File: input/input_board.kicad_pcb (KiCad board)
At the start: 4 copper layers, 271.6 x 100 mm, 233 parts, among them J1 Sensor, J101 Gain, J102 +IN, J103 -IN, J2 SCKB, J3 Decimate, J4 SCKA, J5 MCLK, J6 SDOB1, P1 my_pcie_8x, Q1 NSS1C300ET4G, Q2 2STD1665T4, Q3 NSS1C300ET4G, U1 DS90LV048, U101 AD8599, U102 LTC2512-24, U104 THS4131, U2 FIN1047, U3 OP27, U4 OPA830, U5 74LVC541A, U6 OPA830, U7 MCP1755S-3302E/DB, U8 NCP1117STAT3G, U9 OPA1679, X1 channel_dummy, X2 channel_dummy

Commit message: Input board is nearly ready to send off for the first spin.
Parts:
- removed X1, X2: channel_dummy, input:channel_dummy
- added C201: 330uF, Capacitor_SMD:CP_Elec_8x6.7, F.Cu at (118.2, 106.0)
- added C202: 330uF, Capacitor_SMD:CP_Elec_8x6.7, F.Cu at (118.2, 90.0)
- added C203: 33nF, Capacitor_SMD:C_0805_2012Metric, F.Cu at (133.8, 98.0)
- added C204: 1uF, Capacitor_SMD:C_0805_2012Metric, F.Cu at (142.0, 105.0)
- added C205: 2.2nF, Capacitor_SMD:C_0603_1608Metric, F.Cu at (136.6, 90.4)
- added C206: 2.2nF, Capacitor_SMD:C_0603_1608Metric, F.Cu at (136.6, 105.6)
- added C207: 1uF, Capacitor_SMD:C_0805_2012Metric, F.Cu at (150.0, 98.0)
- added C208: 1uF, Capacitor_SMD:C_0805_2012Metric, F.Cu at (145.6, 105.0)
- added C209: 1uF, Capacitor_SMD:C_0805_2012Metric, F.Cu at (145.5, 91.0)
- added C210: 1uF, Capacitor_SMD:C_0805_2012Metric, F.Cu at (152.0, 88.2)
- added C211: 1uF, Capacitor_SMD:C_0805_2012Metric, F.Cu at (152.0, 107.8)
- added C212: 1nF, Capacitor_SMD:C_0805_2012Metric, F.Cu at (43.5, 96.8)
- added C213: 1nF, Capacitor_SMD:C_0805_2012Metric, F.Cu at (43.5, 99.3)
- added C214: 3.3nF, Capacitor_SMD:C_0805_2012Metric, F.Cu at (75.0, 95.0)
- added C215: 1uF, Capacitor_SMD:C_0805_2012Metric, F.Cu at (78.8, 86.6)
- added C216: 1uF, Capacitor_SMD:C_0805_2012Metric, F.Cu at (81.2, 86.6)
- added C217: 1uF, Capacitor_SMD:C_0805_2012Metric, F.Cu at (81.2, 109.4)
- added C218: 1uF, Capacitor_SMD:C_0805_2012Metric, F.Cu at (78.8, 109.4)
- added C219: 1nF, Capacitor_SMD:C_0805_2012Metric, F.Cu at (85.2, 94.0)
- added C220: 1nF, Capacitor_SMD:C_0805_2012Metric, F.Cu at (85.2, 102.0)
- added C221: 2.2nF, Capacitor_SMD:C_0603_1608Metric, F.Cu at (92.4, 107.0)
- added C222: 2.2nF, Capacitor_SMD:C_0603_1608Metric, F.Cu at (93.6, 90.6)
- added C223: 1uF, Capacitor_SMD:C_0805_2012Metric, F.Cu at (98.2, 98.0)
- added C224: 1uF, Capacitor_SMD:C_0805_2012Metric, F.Cu at (90.6, 91.2)
- added C225: 1uF, Capacitor_SMD:C_0805_2012Metric, F.Cu at (95.6, 105.2)
- added C226: OPT, Capacitor_SMD:C_0805_2012Metric, F.Cu at (163.6, 92.6)
- added C227: 6.8nF, Capacitor_SMD:C_0805_2012Metric, F.Cu at (166.4, 90.4)
- added C228: 6.8nF, Capacitor_SMD:C_0805_2012Metric, F.Cu at (166.4, 94.8)
- added C229: 10uF, Capacitor_SMD:C_0603_1608Metric, F.Cu at (182.4, 88.8)
- added C230: 10uF, Capacitor_SMD:C_0603_1608Metric, F.Cu at (173.0, 89.4)
- added C231: 100nF, Capacitor_SMD:C_0603_1608Metric, F.Cu at (182.4, 90.6)
- added C232: 100nF, Capacitor_SMD:C_0603_1608Metric, F.Cu at (173.0, 91.4)
- added C233: 100nF, Capacitor_SMD:C_0603_1608Metric, F.Cu at (172.9, 94.4)
- added C234: 47uF, Capacitor_SMD:C_1210_3225Metric, F.Cu at (171.9, 96.9)
- added C235: 330uF, Capacitor_SMD:CP_Elec_8x6.7, F.Cu at (174.6, 106.0)
- added C301: 330uF, Capacitor_SMD:CP_Elec_8x6.7, F.Cu at (118.2, 141.1)
- added C302: 330uF, Capacitor_SMD:CP_Elec_8x6.7, F.Cu at (118.2, 125.0)
- added C303: 33nF, Capacitor_SMD:C_0805_2012Metric, F.Cu at (133.8, 133.0)
- added C304: 1uF, Capacitor_SMD:C_0805_2012Metric, F.Cu at (142.0, 140.0)
- added C305: 2.2nF, Capacitor_SMD:C_0603_1608Metric, F.Cu at (136.6, 125.4)
- added C306: 2.2nF, Capacitor_SMD:C_0603_1608Metric, F.Cu at (136.6, 140.6)
- added C307: 1uF, Capacitor_SMD:C_0805_2012Metric, F.Cu at (150.0, 133.0)
- added C308: 1uF, Capacitor_SMD:C_0805_2012Metric, F.Cu at (145.6, 140.0)
- added C309: 1uF, Capacitor_SMD:C_0805_2012Metric, F.Cu at (145.5, 126.0)
- added C310: 1uF, Capacitor_SMD:C_0805_2012Metric, F.Cu at (152.0, 123.2)
- added C311: 1uF, Capacitor_SMD:C_0805_2012Metric, F.Cu at (152.0, 142.8)
- added C312: 1nF, Capacitor_SMD:C_0805_2012Metric, F.Cu at (43.5, 131.8)
- added C313: 1nF, Capacitor_SMD:C_0805_2012Metric, F.Cu at (43.5, 134.3)
- added C314: 3.3nF, Capacitor_SMD:C_0805_2012Metric, F.Cu at (75.0, 130.0)
- added C315: 1uF, Capacitor_SMD:C_0805_2012Metric, F.Cu at (78.8, 121.6)
- added C316: 1uF, Capacitor_SMD:C_0805_2012Metric, F.Cu at (81.2, 121.6)
- added C317: 1uF, Capacitor_SMD:C_0805_2012Metric, F.Cu at (81.2, 144.4)
- added C318: 1uF, Capacitor_SMD:C_0805_2012Metric, F.Cu at (78.8, 144.4)
- added C319: 1nF, Capacitor_SMD:C_0805_2012Metric, F.Cu at (85.2, 129.0)
- added C320: 1nF, Capacitor_SMD:C_0805_2012Metric, F.Cu at (85.2, 137.0)
- added C321: 2.2nF, Capacitor_SMD:C_0603_1608Metric, F.Cu at (92.4, 142.0)
- added C322: 2.2nF, Capacitor_SMD:C_0603_1608Metric, F.Cu at (93.6, 125.6)
- added C323: 1uF, Capacitor_SMD:C_0805_2012Metric, F.Cu at (98.2, 133.0)
- added C324: 1uF, Capacitor_SMD:C_0805_2012Metric, F.Cu at (90.6, 126.2)
- added C325: 1uF, Capacitor_SMD:C_0805_2012Metric, F.Cu at (95.6, 140.2)
- added C326: OPT, Capacitor_SMD:C_0805_2012Metric, F.Cu at (163.6, 127.6)
- added C327: 6.8nF, Capacitor_SMD:C_0805_2012Metric, F.Cu at (166.4, 125.4)
- added C328: 6.8nF, Capacitor_SMD:C_0805_2012Metric, F.Cu at (166.4, 129.8)
- added C329: 10uF, Capacitor_SMD:C_0603_1608Metric, F.Cu at (182.4, 123.8)
- added C330: 10uF, Capacitor_SMD:C_0603_1608Metric, F.Cu at (173.0, 124.4)
- added C331: 100nF, Capacitor_SMD:C_0603_1608Metric, F.Cu at (182.4, 125.6)
- added C332: 100nF, Capacitor_SMD:C_0603_1608Metric, F.Cu at (173.0, 126.4)
- added C333: 100nF, Capacitor_SMD:C_0603_1608Metric, F.Cu at (172.9, 129.4)
- added C334: 47uF, Capacitor_SMD:C_1210_3225Metric, F.Cu at (171.9, 131.9)
- added C335: 330uF, Capacitor_SMD:CP_Elec_8x6.7, F.Cu at (174.6, 142.0)
- added D201: BAS21S, Package_TO_SOT_SMD:SOT-23, F.Cu at (152.0, 104.4)
- added D202: 5V (standoff), Diode_SMD:D_SMA, F.Cu at (167.0, 107.0)
- added D203: 12V, Diode_SMD:D_SOD-323, F.Cu at (55.0, 94.2)
- added D204: 12V, Diode_SMD:D_SOD-323, F.Cu at (55.0, 101.8)
- added D205: BAS21S, Package_TO_SOT_SMD:SOT-23, F.Cu at (80.0, 90.8)
- added D206: BAS21S, Package_TO_SOT_SMD:SOT-23, F.Cu at (80.0, 105.2)
- added D207: BAS21S, Package_TO_SOT_SMD:SOT-23, F.Cu at (64.0, 108.4)
- added D208: BAS21S, Package_TO_SOT_SMD:SOT-23, F.Cu at (59.8, 108.4)
- added D209: BAS21S, Package_TO_SOT_SMD:SOT-23, F.Cu at (64.0, 87.6)
- added D210: BAS21S, Package_TO_SOT_SMD:SOT-23, F.Cu at (59.8, 87.6)
- added D211: BAS21S, Package_TO_SOT_SMD:SOT-23, F.Cu at (152.0, 91.6)
- added D301: BAS21S, Package_TO_SOT_SMD:SOT-23, F.Cu at (152.0, 126.6)
- added D302: BAS21S, Package_TO_SOT_SMD:SOT-23, F.Cu at (152.0, 139.4)
- added D303: 5V (standoff), Diode_SMD:D_SMA, F.Cu at (166.6, 143.0)
- added D304: 12V, Diode_SMD:D_SOD-323, F.Cu at (55.0, 129.2)
- added D305: 12V, Diode_SMD:D_SOD-323, F.Cu at (55.0, 136.8)
- added D306: BAS21S, Package_TO_SOT_SMD:SOT-23, F.Cu at (80.0, 125.8)
- added D307: BAS21S, Package_TO_SOT_SMD:SOT-23, F.Cu at (80.0, 140.2)
- added D308: BAS21S, Package_TO_SOT_SMD:SOT-23, F.Cu at (64.0, 143.4)
- added D309: BAS21S, Package_TO_SOT_SMD:SOT-23, F.Cu at (59.8, 143.4)
- added D310: BAS21S, Package_TO_SOT_SMD:SOT-23, F.Cu at (64.0, 122.6)
- added D311: BAS21S, Package_TO_SOT_SMD:SOT-23, F.Cu at (59.8, 122.6)
- added E201: 2036-07-SMLF, input:GDT_3LINE_Bourns_2036-xx-SM, F.Cu at (36.0, 98.0)
- added E301: 2036-07-SMLF, input:GDT_3LINE_Bourns_2036-xx-SM, F.Cu at (36.0, 133.0)
- added FB201: 21 Ohm, Inductor_SMD:L_0805_2012Metric, F.Cu at (125.2, 91.8)
- added FB202: 21 Ohm, Inductor_SMD:L_0805_2012Metric, F.Cu at (111.4, 107.8)
- added FB203: 2K Ohm, Inductor_SMD:L_0805_2012Metric, F.Cu at (43.5, 94.5)
- added FB204: 2K Ohm, Inductor_SMD:L_0805_2012Metric, F.Cu at (43.5, 101.5)
- added FB205: 21 Ohm, Inductor_SMD:L_0805_2012Metric, F.Cu at (181.4, 109.2)
- added FB301: 21 Ohm, Inductor_SMD:L_0805_2012Metric, F.Cu at (125.2, 126.8)
- added FB302: 21 Ohm, Inductor_SMD:L_0805_2012Metric, F.Cu at (111.4, 142.8)
- added FB303: 2K Ohm, Inductor_SMD:L_0805_2012Metric, F.Cu at (43.5, 129.5)
- added FB304: 2K Ohm, Inductor_SMD:L_0805_2012Metric, F.Cu at (43.5, 136.5)
- added FB305: 21 Ohm, Inductor_SMD:L_0805_2012Metric, F.Cu at (181.4, 144.2)
- added FL201: 4.7mH, input:L_CommonMode_Bourns_DR331, F.Cu at (52.2, 98.0)
- added FL301: 4.7mH, input:L_CommonMode_Bourns_DR331, F.Cu at (52.2, 133.0)
- added J201: Gain, Connector_PinHeader_2.00mm:PinHeader_2x02_P2.00mm_Vertical_SMD, F.Cu at (105.2, 98.0)
- added J202: +IN, Connector_Coaxial:MMCX_Molex_73415-1471_Vertical, F.Cu at (158.5, 87.5)
- added J203: -IN, Connector_Coaxial:MMCX_Molex_73415-1471_Vertical, F.Cu at (158.5, 99.0)
- added J301: Gain, Connector_PinHeader_2.00mm:PinHeader_2x02_P2.00mm_Vertical_SMD, F.Cu at (105.2, 133.0)
- added J302: +IN, Connector_Coaxial:MMCX_Molex_73415-1471_Vertical, F.Cu at (158.5, 122.5)
- added J303: -IN, Connector_Coaxial:MMCX_Molex_73415-1471_Vertical, F.Cu at (158.5, 134.0)
- added R201: 1K, Resistor_SMD:R_0603_1608Metric, F.Cu at (130.0, 93.2)
- added R202: 1K, Resistor_SMD:R_0603_1608Metric, F.Cu at (130.0, 102.8)
- added R203: 698, Resistor_SMD:R_0603_1608Metric, F.Cu at (130.0, 91.0)
- added R204: 698, Resistor_SMD:R_0603_1608Metric, F.Cu at (136.6, 103.4)
- added R205: 3.3K, Resistor_SMD:R_0603_1608Metric, F.Cu at (142.6, 109.2)
- added R206: 3.3K, Resistor_SMD:R_0603_1608Metric, F.Cu at (138.6, 109.2)
- added R207: 1K, Resistor_SMD:R_0603_1608Metric, F.Cu at (136.6, 92.6)
- added R208: 1K, Resistor_SMD:R_0603_1608Metric, F.Cu at (130.0, 105.0)
- added R209: 10, Resistor_SMD:R_0805_2012Metric, F.Cu at (67.6, 93.8)
- added R210: 10, Resistor_SMD:R_0805_2012Metric, F.Cu at (67.6, 102.4)
- added R211: 10, Resistor_SMD:R_0805_2012Metric, F.Cu at (71.6, 93.8)
- added R212: 10, Resistor_SMD:R_0805_2012Metric, F.Cu at (71.6, 102.4)
- added R213: 200K, Resistor_SMD:R_0603_1608Metric, F.Cu at (73.0, 90.8)
- added R214: 200K, Resistor_SMD:R_0603_1608Metric, F.Cu at (69.6, 90.8)
- added R215: 200K, Resistor_SMD:R_0603_1608Metric, F.Cu at (73.0, 105.2)
- added R216: 200K, Resistor_SMD:R_0603_1608Metric, F.Cu at (69.6, 105.2)
- added R217: 200, Resistor_SMD:R_0603_1608Metric, F.Cu at (75.0, 100.6)
- added R218: 10K, Resistor_SMD:R_0603_1608Metric, F.Cu at (69.6, 108.6)
- added R219: 10K, Resistor_SMD:R_0603_1608Metric, F.Cu at (73.0, 108.6)
- added R220: 10K, Resistor_SMD:R_0603_1608Metric, F.Cu at (69.6, 87.4)
- added R221: 10K, Resistor_SMD:R_0603_1608Metric, F.Cu at (73.0, 87.4)
- added R222: 10, Resistor_SMD:R_0805_2012Metric, F.Cu at (81.0, 94.4)
- added R223: 10, Resistor_SMD:R_0805_2012Metric, F.Cu at (81.0, 101.6)
- added R224: 100, Resistor_SMD:R_0603_1608Metric, F.Cu at (107.2, 92.0)
- added R225: 243, Resistor_SMD:R_0603_1608Metric, F.Cu at (103.6, 92.0)
- added R226: 1K, Resistor_SMD:R_0603_1608Metric, F.Cu at (101.0, 98.0)
- added R227: 499, Resistor_SMD:R_0805_2012Metric, F.Cu at (92.4, 104.6)
- added R228: 499, Resistor_SMD:R_0805_2012Metric, F.Cu at (93.8, 88.4)
- added R229: 10, Resistor_SMD:R_0805_2012Metric, F.Cu at (163.6, 88.2)
- added R230: 10, Resistor_SMD:R_0805_2012Metric, F.Cu at (163.6, 96.8)
- added R231: GND lift, Resistor_SMD:R_0603_1608Metric, F.Cu at (158.4, 103.0)
- added R232: 33, Resistor_SMD:R_0603_1608Metric, F.Cu at (187.6, 93.7)
- added R233: 33, Resistor_SMD:R_0603_1608Metric, F.Cu at (184.0, 92.6)
- added R301: 1K, Resistor_SMD:R_0603_1608Metric, F.Cu at (130.0, 128.2)
- added R302: 1K, Resistor_SMD:R_0603_1608Metric, F.Cu at (130.0, 137.8)
- added R303: 698, Resistor_SMD:R_0603_1608Metric, F.Cu at (130.0, 126.0)
- added R304: 698, Resistor_SMD:R_0603_1608Metric, F.Cu at (136.6, 138.4)
- added R305: 3.3K, Resistor_SMD:R_0603_1608Metric, F.Cu at (142.6, 144.2)
- added R306: 3.3K, Resistor_SMD:R_0603_1608Metric, F.Cu at (138.6, 144.2)
- added R307: 1K, Resistor_SMD:R_0603_1608Metric, F.Cu at (136.6, 127.6)
- added R308: 1K, Resistor_SMD:R_0603_1608Metric, F.Cu at (130.0, 140.0)
- added R309: 10, Resistor_SMD:R_0805_2012Metric, F.Cu at (67.6, 128.8)
- added R310: 10, Resistor_SMD:R_0805_2012Metric, F.Cu at (67.6, 137.4)
- added R311: 10, Resistor_SMD:R_0805_2012Metric, F.Cu at (71.6, 128.8)
- added R312: 10, Resistor_SMD:R_0805_2012Metric, F.Cu at (71.6, 137.4)
- added R313: 200K, Resistor_SMD:R_0603_1608Metric, F.Cu at (73.0, 125.8)
- added R314: 200K, Resistor_SMD:R_0603_1608Metric, F.Cu at (69.6, 125.8)
- added R315: 200K, Resistor_SMD:R_0603_1608Metric, F.Cu at (73.0, 140.2)
- added R316: 200K, Resistor_SMD:R_0603_1608Metric, F.Cu at (69.6, 140.2)
- added R317: 200, Resistor_SMD:R_0603_1608Metric, F.Cu at (75.0, 135.6)
- added R318: 10K, Resistor_SMD:R_0603_1608Metric, F.Cu at (69.6, 143.6)
- added R319: 10K, Resistor_SMD:R_0603_1608Metric, F.Cu at (73.0, 143.6)
- added R320: 10K, Resistor_SMD:R_0603_1608Metric, F.Cu at (69.6, 122.4)
- added R321: 10K, Resistor_SMD:R_0603_1608Metric, F.Cu at (73.0, 122.4)
- added R322: 10, Resistor_SMD:R_0805_2012Metric, F.Cu at (81.0, 129.4)
- added R323: 10, Resistor_SMD:R_0805_2012Metric, F.Cu at (81.0, 136.6)
- added R324: 100, Resistor_SMD:R_0603_1608Metric, F.Cu at (107.2, 127.0)
- added R325: 243, Resistor_SMD:R_0603_1608Metric, F.Cu at (103.6, 127.0)
- added R326: 1K, Resistor_SMD:R_0603_1608Metric, F.Cu at (101.0, 133.0)
- added R327: 499, Resistor_SMD:R_0805_2012Metric, F.Cu at (92.4, 139.6)
- added R328: 499, Resistor_SMD:R_0805_2012Metric, F.Cu at (93.8, 123.4)
- added R329: 10, Resistor_SMD:R_0805_2012Metric, F.Cu at (163.6, 123.2)
- added R330: 10, Resistor_SMD:R_0805_2012Metric, F.Cu at (163.6, 131.8)
- added R331: GND lift, Resistor_SMD:R_0603_1608Metric, F.Cu at (158.4, 138.0)
- added R332: 33, Resistor_SMD:R_0603_1608Metric, F.Cu at (184.0, 129.4)
- added R333: 33, Resistor_SMD:R_0603_1608Metric, F.Cu at (184.0, 127.6)
- added TP201: +IN2, TestPoint:TestPoint_THTPad_D1.5mm_Drill0.7mm, F.Cu at (129.5, 86.8)
- added TP202: -IN2, TestPoint:TestPoint_THTPad_D1.5mm_Drill0.7mm, F.Cu at (129.5, 109.0)
- added TP203: -IN1, TestPoint:TestPoint_THTPad_D1.5mm_Drill0.7mm, F.Cu at (86.0, 108.2)
- added TP204: +IN1, TestPoint:TestPoint_THTPad_D1.5mm_Drill0.7mm, F.Cu at (86.0, 87.8)
- added TP205: DRL, TestPoint:TestPoint_THTPad_D1.5mm_Drill0.7mm, F.Cu at (179.4, 99.8)
- added TP206: BUSY, TestPoint:TestPoint_THTPad_D1.5mm_Drill0.7mm, F.Cu at (179.4, 86.4)
- added TP207: GND, TestPoint:TestPoint_THTPad_D1.5mm_Drill0.7mm, F.Cu at (159.2, 93.2)
- added TP208: VREF, TestPoint:TestPoint_THTPad_D1.5mm_Drill0.7mm, F.Cu at (168.3, 102.0)
- added TP209: SDOA, TestPoint:TestPoint_THTPad_D1.5mm_Drill0.7mm, F.Cu at (189.5, 90.0)
- added TP301: +IN2, TestPoint:TestPoint_THTPad_D1.5mm_Drill0.7mm, F.Cu at (129.5, 121.8)
- added TP302: -IN2, TestPoint:TestPoint_THTPad_D1.5mm_Drill0.7mm, F.Cu at (129.5, 144.0)
- added TP303: -IN1, TestPoint:TestPoint_THTPad_D1.5mm_Drill0.7mm, F.Cu at (86.0, 143.2)
- added TP304: +IN1, TestPoint:TestPoint_THTPad_D1.5mm_Drill0.7mm, F.Cu at (86.0, 122.8)
- added TP305: DRL, TestPoint:TestPoint_THTPad_D1.5mm_Drill0.7mm, F.Cu at (179.4, 134.8)
- added TP306: BUSY, TestPoint:TestPoint_THTPad_D1.5mm_Drill0.7mm, F.Cu at (179.4, 121.4)
- added TP307: GND, TestPoint:TestPoint_THTPad_D1.5mm_Drill0.7mm, F.Cu at (159.2, 128.2)
- added TP308: VREF, TestPoint:TestPoint_THTPad_D1.5mm_Drill0.7mm, F.Cu at (168.3, 137.0)
- added TP309: SDOA, TestPoint:TestPoint_THTPad_D1.5mm_Drill0.7mm, F.Cu at (193.0, 133.8)
- added U201: THS4131, Package_SO:SO-8_5.3x6.2mm_P1.27mm, F.Cu at (144.9, 98.0)
- added U202: AD8599, Package_SO:SO-8_5.3x6.2mm_P1.27mm, F.Cu at (93.3, 98.0)
- added U203: LTC2512-24, input:DFN-24-1EP_4x7mm_P0.5mm_EP2.64x6.44mm, F.Cu at (177.3, 93.2)
- added U301: THS4131, Package_SO:SO-8_5.3x6.2mm_P1.27mm, F.Cu at (144.9, 133.0)
- added U302: AD8599, Package_SO:SO-8_5.3x6.2mm_P1.27mm, F.Cu at (93.3, 133.0)
- added U303: LTC2512-24, input:DFN-24-1EP_4x7mm_P0.5mm_EP2.64x6.44mm, F.Cu at (177.3, 128.2)
- U102: footprint Package_DFN_QFN:DFN-24-1EP_4x7mm_P0.5mm_EP2.64x6.44mm -> input:DFN-24-1EP_4x7mm_P0.5mm_EP2.64x6.44mm
- moved J1 29.5 mm to (31.0, 119.5)
- moved C31 27.0 mm to (44.8, 121.8)
- moved D9 27.0 mm to (46.6, 115.2)
- moved FB5 27.0 mm to (44.8, 119.0)
- moved FB6 27.0 mm to (49.0, 121.8)
- moved R21 7.25 mm to (222.5, 89.2)
- moved D101 4.01 mm to (55.0, 63.2)
- moved D102 4.01 mm to (55.0, 70.8)
- moved C120 4.00 mm to (43.5, 65.8)
- moved C121 4.00 mm to (43.5, 68.3)
- moved FB101 4.00 mm to (43.5, 63.5)
- moved FB102 4.00 mm to (43.5, 70.5)
- moved FL101 4.00 mm to (52.2, 67.0)
- moved TP1 4.00 mm to (40.0, 60.2)
- moved TP2 4.00 mm to (40.0, 74.0)
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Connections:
- net Net-(C122-Pad1) renamed /input_channel/in_filter/input+3
- net Net-(D101-Pad1) renamed /input_channel/in_filter/input+1
- net Net-(D102-Pad1) renamed /input_channel/in_filter/input-1
- net Net-(D104-Pad3) renamed /input_channel/in_filter/input-3
- net Net-(R115-Pad1) renamed /input_channel/in_filter/input+2
- net Net-(R116-Pad1) renamed /input_channel/in_filter/input-2
- C10 pad 1: Net-(C10-Pad1) -> GND
- J1 pad 4: /channel_dummy3/+in -> /channel3/+in
- J1 pad 5: /channel_dummy3/-in -> /channel3/-in
- J1 pad 7: /channel_dummy2/-in -> /channel2/-in
- J1 pad 8: /channel_dummy2/+in -> /channel2/+in
- RN1 pad 5: /channel_dummy2/SCKA -> /channel2/SCKA
- RN1 pad 6: /channel_dummy2/MCLK -> /channel2/MCLK
- RN1 pad 7: /channel_dummy3/SCKA -> /channel3/SCKA
- RN1 pad 8: /channel_dummy3/MCLK -> /channel3/MCLK
- U2 pad 6: /channel_dummy2/SDOA -> /channel2/SDOA
- U2 pad 7: /channel_dummy3/SDOA -> /channel3/SDOA
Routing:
- net /channel_dummy3/SDOA: track 261.2 -> 0.00 mm, vias 2 -> 0
- net /channel_dummy3/SCKA: track 255.4 -> 0.00 mm
- net /channel_dummy3/MCLK: track 250.0 -> 0.00 mm
- net GND: track 521.8 -> 757.4 mm, vias 186 -> 403
- net /channel_dummy2/SDOA: track 224.2 -> 0.00 mm, vias 2 -> 0
- net /channel_dummy2/MCLK: track 217.0 -> 0.00 mm
- net /channel_dummy2/SCKA: track 212.4 -> 0.00 mm
- net V+: track 389.6 -> 557.5 mm, vias 12 -> 23
- net /channel3/SDOA: track 0.00 -> 148.4 mm, vias 0 -> 4
- net /channel3/MCLK: track 0.00 -> 126.0 mm
- net /channel3/SCKA: track 0.00 -> 123.7 mm
- net /channel2/SDOA: track 0.00 -> 110.1 mm, vias 0 -> 2
- net /channel2/ADC/CHAN_VREF: track 0.00 -> 106.8 mm, vias 0 -> 27
- net /channel3/ADC/CHAN_VREF: track 0.00 -> 106.8 mm, vias 0 -> 26
- net /channel2/SCKA: track 0.00 -> 94.3 mm
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- added copper zone on F.Cu, net /channel2/ADC/CHAN_VREF
- added copper zone on In2.Cu, net /channel2/ADC/CHAN_VREF
- added copper zone on B.Cu, net /channel2/ADC/J102_J103_GND
- added copper zone on In2.Cu, net /channel2/CHAN_V+
- added copper zone on In2.Cu, net /channel2/CHAN_V-
- added copper zone on F.Cu, net /channel3/ADC/CHAN_VREF
- added copper zone on In2.Cu, net /channel3/ADC/CHAN_VREF
- added copper zone on B.Cu, net /channel3/ADC/J102_J103_GND
- added copper zone on In2.Cu, net /channel3/CHAN_V+
- added copper zone on In2.Cu, net /channel3/CHAN_V-
- added copper zone on F.Cu, net Earth
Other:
- net class 50 Ohm: trace_width 0.36 -> 0.3
- net class Fast: trace_width 0.15 -> 0.2; via_dia 0.45 -> 0.4572; via_drill 0.2 -> 0.254
- net class Input added: clearance 0.2, trace_width 0.5, via_dia 0.6, via_drill 0.3
- net class LVDS: via_dia 0.45 -> 0.4572; via_drill 0.2 -> 0.254
- net class Slow: via_dia 0.45 -> 0.4572; via_drill 0.2 -> 0.254
- rule trace_min: 0.1016 -> 0.127
- rule via_min_drill: 0.2 -> 0.254
- rule via_min_size: 0.45 -> 0.4572

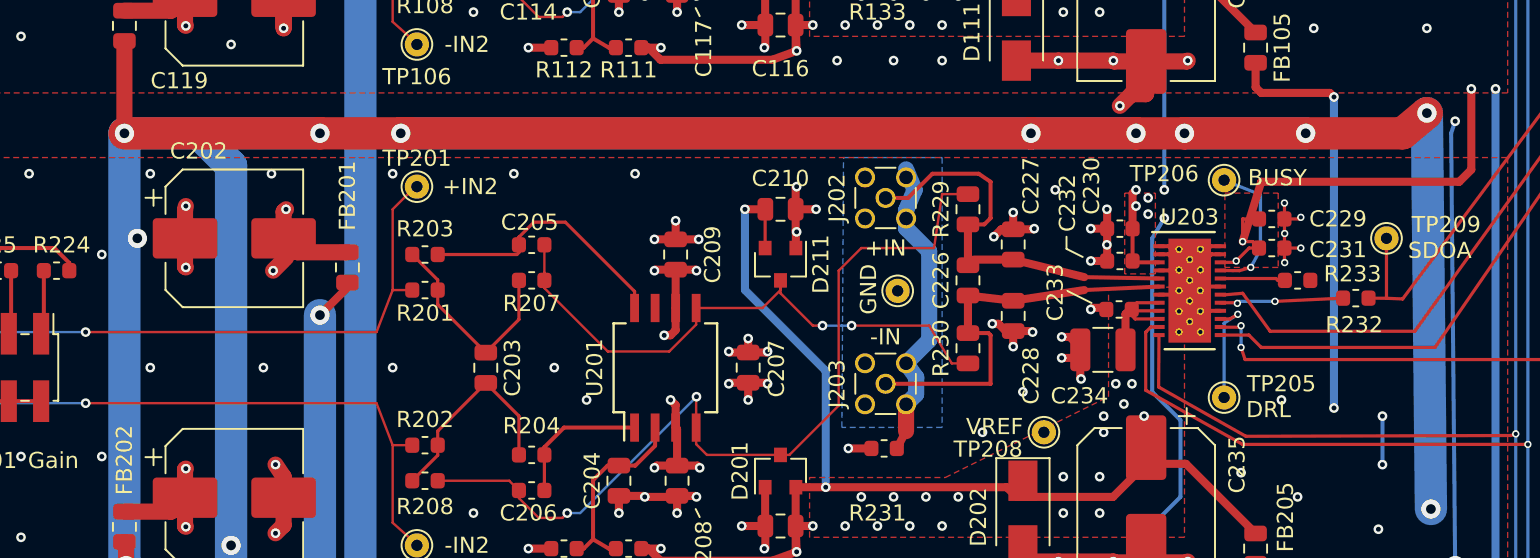
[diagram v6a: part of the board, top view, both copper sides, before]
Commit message: Changed the input TVS from 12V bidirectional to 8V unidirectional, board tweaks
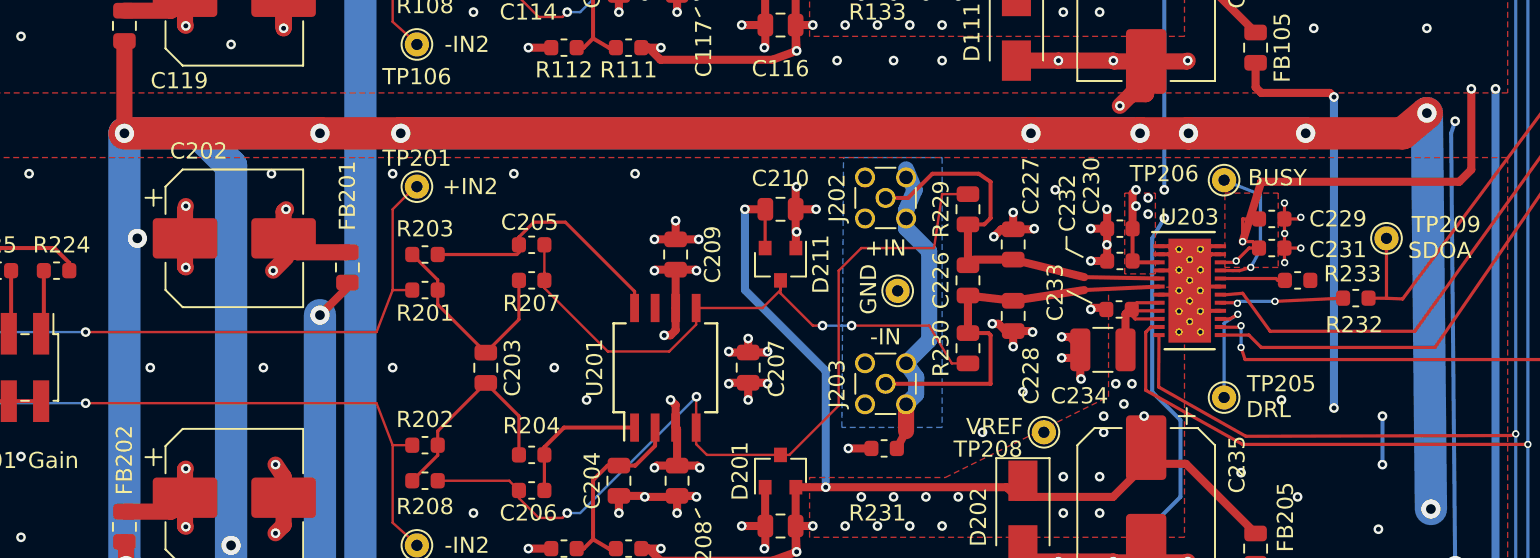
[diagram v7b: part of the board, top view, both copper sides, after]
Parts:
- D101, D102, D203, D204, D304, D305: value 12V -> 8V
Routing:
- net GND: vias 403 -> 400

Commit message: Various tweaks to schematic which help in the PCB view, mainly getting informative net names. Also unscrambled the + and - paths in the input channel.  This avoided a cross-over before the first stage, and an unintended inversion, but mostly just made net naming less confusing.
Getting better net names made it easier to review the PCB to see if it made sense.  I checked
the ICs on the PCB against the datasheet pinout, and while doing this fixed an actual bug where
I had BIST-+ and BIST+-swapped.

I made some tweaks on the PCB to try to equalize the copper area on the input nets so as to
match the capacitance.  I tweaked the top-side ground pours somewhat, adding in the regulator
area, removing around the high speed traces.

Some changes from gerber viewing.  I reduced the solder mask clearances so that we get mask
web between the SOIC and DFN pads.  I reduced the pad size of the big via from 1.2 to 1.0 mm.
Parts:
- moved C32 1.25 mm to (200.8, 145.1)
- moved TP107 0.40 mm to (86.4, 77.2)
- moved TP108 0.40 mm to (86.4, 56.8)
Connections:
- net /channel2/ADC/+in renamed /channel2/ADC/+IN_ADC
- net /channel2/ADC/-in renamed /channel2/ADC/-IN_ADC
- net /channel2/antialias_driver/+in renamed /channel2/antialias_driver/-IN2
- net /channel2/antialias_driver/-in renamed /channel2/antialias_driver/+IN2
- net /channel3/ADC/+in renamed /channel3/ADC/+IN_ADC
- net /channel3/ADC/-in renamed /channel3/ADC/-IN_ADC
- net /channel3/antialias_driver/+in renamed /channel3/antialias_driver/-IN2
- net /channel3/antialias_driver/-in renamed /channel3/antialias_driver/+IN2
- net /input_channel/ADC/+in renamed /input_channel/ADC/+IN_ADC
- net /input_channel/ADC/-in renamed /input_channel/ADC/-IN_ADC
- net /input_channel/antialias_driver/+in renamed /input_channel/antialias_driver/-IN2
- net /input_channel/antialias_driver/-in renamed /input_channel/antialias_driver/+IN2
- net Net-(C1-Pad2) renamed /reference_buffer/U3+
- net Net-(C10-Pad2) renamed /power/U6V-
- net Net-(C101-Pad1) renamed /input_channel/ADC/ADC_IN+
- net Net-(C101-Pad2) renamed /input_channel/ADC/ADC_IN-
- net Net-(C111-Pad1) renamed /input_channel/antialias_driver/FILTER+
- net Net-(C111-Pad2) renamed /input_channel/antialias_driver/FILTER-
- net Net-(C112-Pad2) renamed /input_channel/antialias_driver/Ux04VIN+
- net Net-(C114-Pad2) renamed /input_channel/antialias_driver/Ux04VIN-
- net Net-(C115-Pad2) renamed /input_channel/antialias_driver/VOCM
- net Net-(C12-Pad1) renamed /power/U4-
- net Net-(C12-Pad2) renamed /power/Q2E
- net Net-(C129-Pad2) renamed /input_channel/in_amp/Ux01A-
- net Net-(C13-Pad1) renamed /power/U6-
- net Net-(C13-Pad2) renamed /power/Q3E
- net Net-(C130-Pad2) renamed /input_channel/in_amp/Ux01B-
- net Net-(C2-Pad1) renamed /reference_buffer/U3-
- net Net-(C203-Pad1) renamed /channel2/antialias_driver/FILTER+
- net Net-(C203-Pad2) renamed /channel2/antialias_driver/FILTER-
- net Net-(C204-Pad2) renamed /channel2/antialias_driver/VOCM
- net Net-(C205-Pad2) renamed /channel2/antialias_driver/Ux04VIN+
- net Net-(C206-Pad2) renamed /channel2/antialias_driver/Ux04VIN-
- net Net-(C22-Pad2) renamed /power/U7IN
- net Net-(C221-Pad2) renamed /channel2/in_amp/Ux01A-
- net Net-(C222-Pad2) renamed /channel2/in_amp/Ux01B-
- net Net-(C226-Pad1) renamed /channel2/ADC/ADC_IN+
- net Net-(C226-Pad2) renamed /channel2/ADC/ADC_IN-
- net Net-(C23-Pad2) renamed /power/U8IN
- net Net-(C3-Pad2) renamed /reference_buffer/U3V+
- net Net-(C303-Pad1) renamed /channel3/antialias_driver/FILTER+
- net Net-(C303-Pad2) renamed /channel3/antialias_driver/FILTER-
- net Net-(C304-Pad2) renamed /channel3/antialias_driver/VOCM
- net Net-(C305-Pad2) renamed /channel3/antialias_driver/Ux04VIN+
- net Net-(C306-Pad2) renamed /channel3/antialias_driver/Ux04VIN-
- net Net-(C321-Pad2) renamed /channel3/in_amp/Ux01A-
- net Net-(C322-Pad2) renamed /channel3/in_amp/Ux01B-
- net Net-(C326-Pad1) renamed /channel3/ADC/ADC_IN+
- net Net-(C326-Pad2) renamed /channel3/ADC/ADC_IN-
- net Net-(C35-Pad2) renamed /bist_buffer/U9A+
- net Net-(C36-Pad2) renamed /bist_buffer/U9C+
- net Net-(C37-Pad2) renamed /bist_buffer/U9B+
- net Net-(C38-Pad2) renamed /bist_buffer/U9D+
- net Net-(C4-Pad2) renamed /reference_buffer/U3V-
- net Net-(C7-Pad1) renamed /power/U4V+
- net Net-(C9-Pad2) renamed /power/U6V+
- net Net-(D1-Pad3) renamed /reference_buffer/U3OUT
- net Net-(R11-Pad1) renamed /power/U6+
- net Net-(R17-Pad2) renamed /power/U4OUT
- net Net-(R18-Pad2) renamed /power/U6OUT
- net Net-(R8-Pad1) renamed /power/U4+
- C127 pad 1: /input_channel/in_amp/+in -> /input_channel/in_amp/+IN1
- C128 pad 1: /input_channel/in_amp/-in -> /input_channel/in_amp/-IN1
- C219 pad 1: /channel2/in_amp/+in -> /channel2/in_amp/+IN1
- C220 pad 1: /channel2/in_amp/-in -> /channel2/in_amp/-IN1
- C319 pad 1: /channel3/in_amp/+in -> /channel3/in_amp/+IN1
- C320 pad 1: /channel3/in_amp/-in -> /channel3/in_amp/-IN1
- R124 pad 1: /input_channel/in_amp/+in -> /input_channel/in_amp/+IN1
- R125 pad 1: /input_channel/in_amp/-in -> /input_channel/in_amp/-IN1
- R222 pad 1: /channel2/in_amp/+in -> /channel2/in_amp/+IN1
- R223 pad 1: /channel2/in_amp/-in -> /channel2/in_amp/-IN1
- R322 pad 1: /channel3/in_amp/+in -> /channel3/in_amp/+IN1
- R323 pad 1: /channel3/in_amp/-in -> /channel3/in_amp/-IN1
- TP107 pad 1: /input_channel/in_amp/-in -> /input_channel/in_amp/-IN1
- TP108 pad 1: /input_channel/in_amp/+in -> /input_channel/in_amp/+IN1
- TP203 pad 1: /channel2/in_amp/-in -> /channel2/in_amp/-IN1
- TP204 pad 1: /channel2/in_amp/+in -> /channel2/in_amp/+IN1
- TP303 pad 1: /channel3/in_amp/-in -> /channel3/in_amp/-IN1
- TP304 pad 1: /channel3/in_amp/+in -> /channel3/in_amp/+IN1
- U101 pad 3: /input_channel/in_amp/+in -> /input_channel/in_amp/-IN1
- U101 pad 5: /input_channel/in_amp/-in -> /input_channel/in_amp/+IN1
- U202 pad 3: /channel2/in_amp/+in -> /channel2/in_amp/-IN1
- U202 pad 5: /channel2/in_amp/-in -> /channel2/in_amp/+IN1
- U302 pad 3: /channel3/in_amp/+in -> /channel3/in_amp/-IN1
- U302 pad 5: /channel3/in_amp/-in -> /channel3/in_amp/+IN1
- U9 pad 7: BIST-+ -> BIST+-
- U9 pad 8: BIST+- -> BIST-+
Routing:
- net /channel3/in_amp/+IN1: track 0.00 -> 26.3 mm
- net /input_channel/in_amp/+IN1: track 0.00 -> 26.3 mm
- net /channel2/in_amp/+IN1: track 0.00 -> 26.3 mm
- net /channel3/in_amp/-in: track 25.8 -> 0.00 mm
- net /input_channel/in_amp/-in: track 25.8 -> 0.00 mm
- net /channel2/in_amp/-in: track 25.8 -> 0.00 mm
- net /channel3/in_amp/+in: track 25.8 -> 0.00 mm, vias 2 -> 0
- net /input_channel/in_amp/+in: track 25.8 -> 0.00 mm, vias 2 -> 0
- net /channel2/in_amp/+in: track 25.8 -> 0.00 mm, vias 2 -> 0
- net /input_channel/in_amp/-IN1: track 0.00 -> 25.1 mm
- net /channel2/in_amp/-IN1: track 0.00 -> 25.0 mm
- net /channel3/in_amp/-IN1: track 0.00 -> 25.0 mm
- net /channel3/+in: track 22.4 -> 38.6 mm
- net /channel2/-in: track 21.0 -> 30.8 mm
- net BIST+-: track 87.9 -> 96.7 mm
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- added copper zone on B.Cu, net Earth
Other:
- rule pad_to_mask_clearance: 0.051 -> 0.0381
- rule solder_mask_min_width: 0.25 -> 0.1016
